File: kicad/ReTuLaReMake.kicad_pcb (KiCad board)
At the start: 2 copper layers, 54 x 26 mm, 23 parts, among them J1 40 Pin DIP Header, U1 ATF1508AS-10AU100

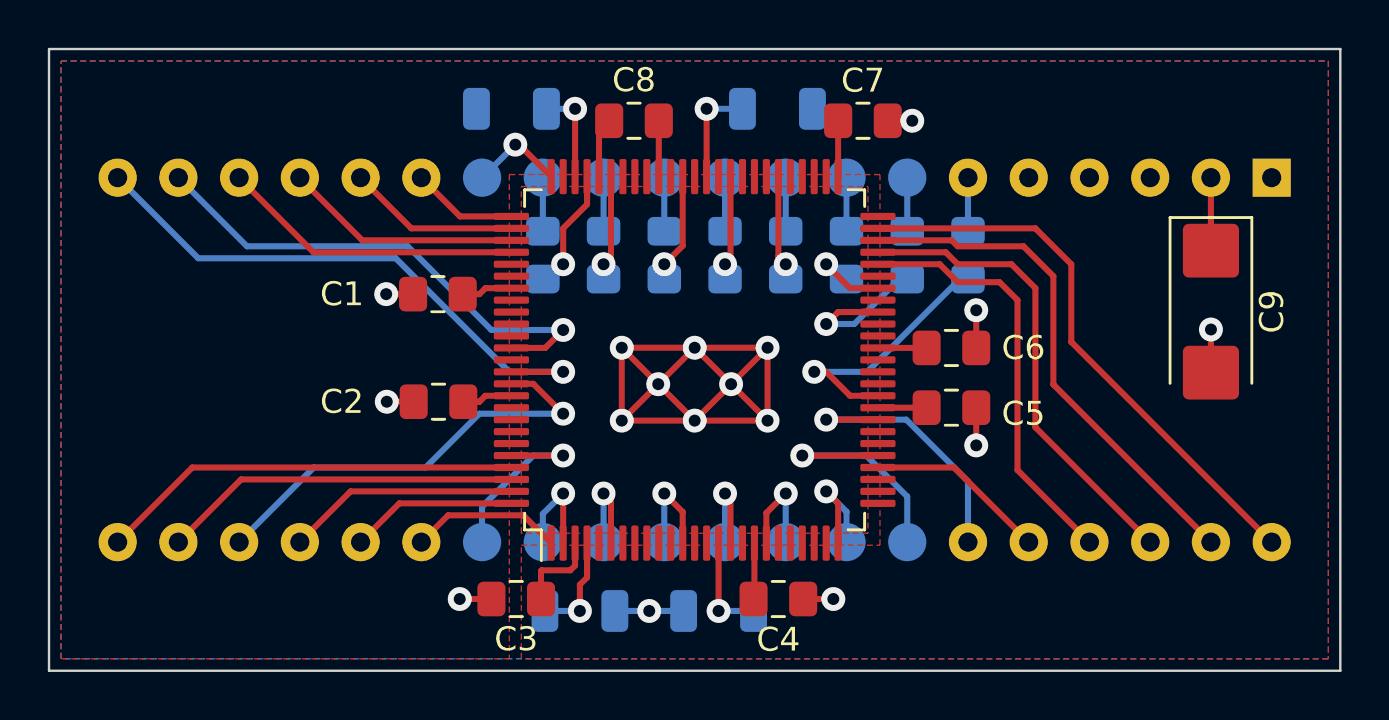
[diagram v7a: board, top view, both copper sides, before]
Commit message: KiCad: Move p_rd_b to a global clock
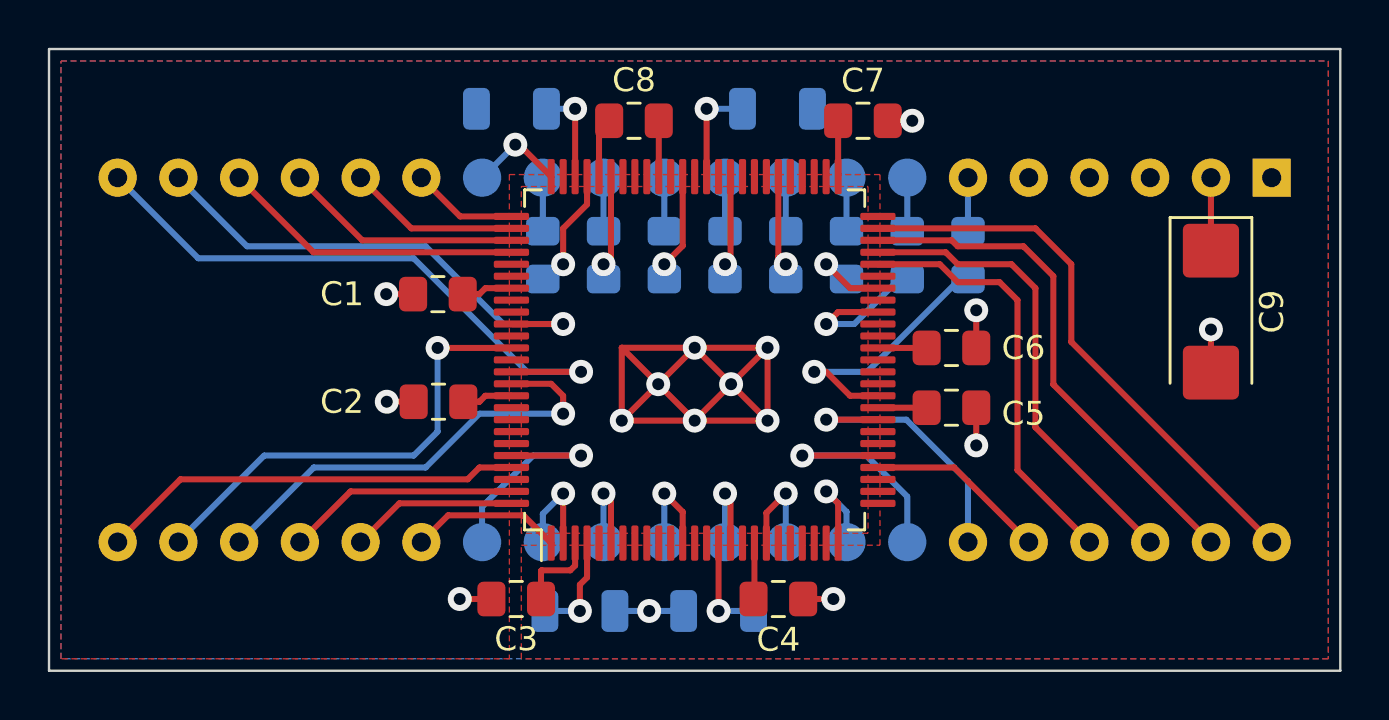
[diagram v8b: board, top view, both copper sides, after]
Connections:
- U1 pad 85: GND -> /HO2
- U1 pad 87: /HO2 -> /PNRDS
- U1 pad 98: /PNRDS -> GND
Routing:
- net /PNRDS: track 15.0 -> 19.4 mm, vias 0 -> 1
- net /PA0: track 7.92 -> 9.42 mm
- net /HRST: track 24.2 -> 25.7 mm
- net GND: vias 16 -> 15
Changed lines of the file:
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@@
   (net 46 "/HD6")
   (net 47 "/HD7")
-  (net 48 "Net-(U1-Pad62)")
-  (net 49 "Net-(U1-Pad73)")
+  (net 48 "Net-(R9-Pad1)")
+  (net 49 "Net-(R10-Pad1)")
   (net 50 "Net-(R11-Pad1)")
   (net 51 "unconnected-(R10-Pad2)")
@@
       (net 2 "GND") (pinfunction "I/O_47") (pintype "passive"))
     (pad "62" smd roundrect (at 7.6625 0.5 90) (size 1.475 0.3) (layers "F.Cu" "F.Paste" "F.Mask") (roundrect_rratio 0.25)
-      (net 48 "Net-(U1-Pad62)") (pinfunction "I/O/TCK") (pintype "passive"))
+      (net 48 "Net-(R9-Pad1)") (pinfunction "I/O/TCK") (pintype "passive"))
     (pad "63" smd roundrect (at 7.6625 0 90) (size 1.475 0.3) (layers "F.Cu" "F.Paste" "F.Mask") (roundrect_rratio 0.25)
       (net 2 "GND") (pinfunction "I/O_48") (pintype "passive"))
@@
       (net 47 "/HD7") (pinfunction "I/O_56") (pintype "passive"))
     (pad "73" smd roundrect (at 7.6625 -5 90) (size 1.475 0.3) (layers "F.Cu" "F.Paste" "F.Mask") (roundrect_rratio 0.25)
-      (net 49 "Net-(U1-Pad73)") (pinfunction "I/O/TDO") (pintype "passive"))
+      (net 49 "Net-(R10-Pad1)") (pinfunction "I/O/TDO") (pintype "passive"))
     (pad "74" smd roundrect (at 7.6625 -5.5 90) (size 1.475 0.3) (layers "F.Cu" "F.Paste" "F.Mask") (roundrect_rratio 0.25)
       (net 2 "GND") (pinfunction "GND_6") (pintype "passive"))
@@
       (net 2 "GND") (pinfunction "I/O_65") (pintype "passive"))
     (pad "85" smd roundrect (at 1.5 -7.6625 90) (size 0.3 1.475) (layers "F.Cu" "F.Paste" "F.Mask") (roundrect_rratio 0.25)
-      (net 2 "GND") (pinfunction "I/O/GCLK3") (pintype "passive"))
+      (net 18 "/HO2") (pinfunction "I/O/GCLK3") (pintype "passive"))
     (pad "86" smd roundrect (at 1 -7.6625 90) (size 0.3 1.475) (layers "F.Cu" "F.Paste" "F.Mask") (roundrect_rratio 0.25)
       (net 2 "GND") (pinfunction "GND_7") (pintype "passive"))
     (pad "87" smd roundrect (at 0.5 -7.6625 90) (size 0.3 1.475) (layers "F.Cu" "F.Paste" "F.Mask") (roundrect_rratio 0.25)
-      (net 18 "/HO2") (pinfunction "INPUT/GCLK1") (pintype "passive"))
+      (net 21 "/PNRDS") (pinfunction "INPUT/GCLK1") (pintype "passive"))
     (pad "88" smd roundrect (at 0 -7.6625 90) (size 0.3 1.475) (layers "F.Cu" "F.Paste" "F.Mask") (roundrect_rratio 0.25)
       (net 2 "GND") (pinfunction "INPUT/OE1") (pintype "passive"))
@@
       (net 20 "/PCS") (pinfunction "I/O_70") (pintype "passive"))
     (pad "98" smd roundrect (at -5 -7.6625 90) (size 0.3 1.475) (layers "F.Cu" "F.Paste" "F.Mask") (roundrect_rratio 0.25)
-      (net 21 "/PNRDS") (pinfunction "I/O_71") (pintype "passive"))
+      (net 2 "GND") (pinfunction "I/O_71") (pintype "passive"))
     (pad "99" smd roundrect (at -5.5 -7.6625 90) (size 0.3 1.475) (layers "F.Cu" "F.Paste" "F.Mask") (roundrect_rratio 0.25)
       (net 23 "/DACK") (pinfunction "I/O_72") (pintype "passive"))
@@
     (fp_line (start 1.6 0.8) (end 1.6 -0.8) (layer "B.Fab") (width 0.1))
     (pad "1" smd roundrect (at -1.4625 0 180) (size 1.125 1.75) (layers "B.Cu" "B.Paste" "B.Mask") (roundrect_rratio 0.2222222222)
-      (net 49 "Net-(U1-Pad73)") (pintype "passive"))
+      (net 49 "Net-(R10-Pad1)") (pintype "passive"))
     (pad "2" smd roundrect (at 1.4625 0 180) (size 1.125 1.75) (layers "B.Cu" "B.Paste" "B.Mask") (roundrect_rratio 0.2222222222)
       (net 51 "unconnected-(R10-Pad2)") (pintype "passive+no_connect"))
@@
     (fp_line (start 1.6 -0.8) (end -1.6 -0.8) (layer "B.Fab") (width 0.1))
     (pad "1" smd roundrect (at -1.4625 0) (size 1.125 1.75) (layers "B.Cu" "B.Paste" "B.Mask") (roundrect_rratio 0.2222222222)
-      (net 48 "Net-(U1-Pad62)") (pintype "passive"))
+      (net 48 "Net-(R9-Pad1)") (pintype "passive"))
     (pad "2" smd roundrect (at 1.4625 0) (size 1.125 1.75) (layers "B.Cu" "B.Paste" "B.Mask") (roundrect_rratio 0.2222222222)
       (net 2 "GND") (pintype "passive"))
@@
   (via (at 130.048 121.92) (size 1) (drill 0.5) (layers "F.Cu" "B.Cu") (free) (net 2))
   (via (at 136.1 109.38) (size 1) (drill 0.5) (layers "F.Cu" "B.Cu") (net 2))
-  (via (at 123.952 118.872) (size 1) (drill 0.5) (layers "F.Cu" "B.Cu") (free) (net 2))
   (via (at 128.524 120.396) (size 1) (drill 0.5) (layers "F.Cu" "B.Cu") (free) (net 2))
   (via (at 123.952 121.92) (size 1) (drill 0.5) (layers "F.Cu" "B.Cu") (free) (net 2))
@@
   (segment (start 107.945 111.765) (end 111.06 114.88) (width 0.254) (layer "F.Cu") (net 17))
   (segment (start 111.06 114.88) (end 119.3375 114.88) (width 0.254) (layer "F.Cu") (net 17))
-  (segment (start 121.5 118.13) (end 120.75 118.88) (width 0.254) (layer "F.Cu") (net 18))
-  (segment (start 120.75 118.88) (end 119.3375 118.88) (width 0.254) (layer "F.Cu") (net 18))
-  (via (at 121.5 118.13) (size 1) (drill 0.5) (layers "F.Cu" "B.Cu") (net 18))
-  (segment (start 115 114.63) (end 108.28 114.63) (width 0.254) (layer "B.Cu") (net 18))
-  (segment (start 121.5 118.13) (end 118.5 118.13) (width 0.254) (layer "B.Cu") (net 18))
-  (segment (start 118.5 118.13) (end 115 114.63) (width 0.254) (layer "B.Cu") (net 18))
+  (segment (start 121.5 117.88) (end 119.3375 117.88) (width 0.254) (layer "F.Cu") (net 18))
+  (via (at 121.5 117.88) (size 1) (drill 0.5) (layers "F.Cu" "B.Cu") (net 18))
+  (segment (start 121.5 117.88) (end 119 117.88) (width 0.254) (layer "B.Cu") (net 18))
+  (segment (start 119 117.88) (end 115.75 114.63) (width 0.254) (layer "B.Cu") (net 18))
   (segment (start 108.28 114.63) (end 105.41 111.76) (width 0.254) (layer "B.Cu") (net 18))
-  (segment (start 121.5 119.88) (end 119.3375 119.88) (width 0.254) (layer "F.Cu") (net 19))
-  (via (at 121.5 119.88) (size 1) (drill 0.5) (layers "F.Cu" "B.Cu") (net 19))
-  (segment (start 114.5 115.13) (end 119.25 119.88) (width 0.254) (layer "B.Cu") (net 19))
-  (segment (start 119.25 119.88) (end 121.5 119.88) (width 0.254) (layer "B.Cu") (net 19))
-  (segment (start 106.24 115.13) (end 114.5 115.13) (width 0.254) (layer "B.Cu") (net 19))
-  (segment (start 102.87 111.76) (end 106.24 115.13) (width 0.254) (layer "B.Cu") (net 19))
-  (segment (start 119.3375 123.88) (end 105.99 123.88) (width 0.254) (layer "F.Cu") (net 20))
-  (segment (start 102.865 127.005) (end 105.99 123.88) (width 0.254) (layer "F.Cu") (net 20))
-  (segment (start 108.03 124.38) (end 105.405 127.005) (width 0.254) (layer "F.Cu") (net 21))
-  (segment (start 119.3375 124.38) (end 108.03 124.38) (width 0.254) (layer "F.Cu") (net 21))
-  (segment (start 120.25 120.38) (end 119.3375 120.38) (width 0.254) (layer "F.Cu") (net 22))
-  (segment (start 121.5 121.63) (end 120.25 120.38) (width 0.254) (layer "F.Cu") (net 22))
+  (segment (start 115.75 114.63) (end 108.28 114.63) (width 0.254) (layer "B.Cu") (net 18))
+  (segment (start 122.25 119.88) (end 119.3375 119.88) (width 0.254) (layer "F.Cu") (net 19))
+  (via (at 122.25 119.88) (size 1) (drill 0.5) (layers "F.Cu" "B.Cu") (net 19))
+  (segment (start 106.24 115.13) (end 102.87 111.76) (width 0.254) (layer "B.Cu") (net 19))
+  (segment (start 120 119.88) (end 115.25 115.13) (width 0.254) (layer "B.Cu") (net 19))
+  (segment (start 122.25 119.88) (end 120 119.88) (width 0.254) (layer "B.Cu") (net 19))
+  (segment (start 115.25 115.13) (end 106.24 115.13) (width 0.254) (layer "B.Cu") (net 19))
+  (segment (start 105.495 124.375) (end 102.865 127.005) (width 0.254) (layer "F.Cu") (net 20))
+  (segment (start 119.3375 123.88) (end 118 123.88) (width 0.254) (layer "F.Cu") (net 20))
+  (segment (start 117.505 124.375) (end 105.495 124.375) (width 0.254) (layer "F.Cu") (net 20))
+  (segment (start 118 123.88) (end 117.505 124.375) (width 0.254) (layer "F.Cu") (net 20))
+  (segment (start 119.3375 118.88) (end 116.25 118.88) (width 0.254) (layer "F.Cu") (net 21))
+  (via (at 116.25 118.88) (size 1) (drill 0.5) (layers "F.Cu" "B.Cu") (net 21))
+  (segment (start 105.41 127) (end 105.41 126.97) (width 0.254) (layer "B.Cu") (net 21))
+  (segment (start 105.41 126.97) (end 109 123.38) (width 0.254) (layer "B.Cu") (net 21))
+  (segment (start 115.25 123.38) (end 116.25 122.38) (width 0.254) (layer "B.Cu") (net 21))
+  (segment (start 109 123.38) (end 115.25 123.38) (width 0.254) (layer "B.Cu") (net 21))
+  (segment (start 116.25 118.88) (end 116.25 122.38) (width 0.254) (layer "B.Cu") (net 21))
+  (segment (start 121 120.38) (end 119.3375 120.38) (width 0.254) (layer "F.Cu") (net 22))
+  (segment (start 121.5 120.88) (end 121 120.38) (width 0.254) (layer "F.Cu") (net 22))
+  (segment (start 121.5 121.63) (end 121.5 120.88) (width 0.254) (layer "F.Cu") (net 22))
   (via (at 121.5 121.63) (size 1) (drill 0.5) (layers "F.Cu" "B.Cu") (net 22))
   (segment (start 111.07 123.88) (end 107.95 127) (width 0.254) (layer "B.Cu") (net 22))
@@
   (segment (start 119.8375 125.88) (end 121 127.0425) (width 0.254) (layer "F.Cu") (net 25))
   (segment (start 116.69 125.88) (end 119.8375 125.88) (width 0.254) (layer "F.Cu") (net 25))
-  (segment (start 119.3375 123.38) (end 121.5 123.38) (width 0.254) (layer "F.Cu") (net 26))
-  (via (at 121.5 123.38) (size 1) (drill 0.5) (layers "F.Cu" "B.Cu") (net 26))
-  (segment (start 121.5 123.38) (end 120.25 123.38) (width 0.254) (layer "B.Cu") (net 26))
+  (segment (start 119.3375 123.38) (end 122.25 123.38) (width 0.254) (layer "F.Cu") (net 26))
+  (via (at 122.25 123.38) (size 1) (drill 0.5) (layers "F.Cu" "B.Cu") (net 26))
   (segment (start 118.11 125.52) (end 118.11 127) (width 0.254) (layer "B.Cu") (net 26))
+  (segment (start 122.25 123.38) (end 120.25 123.38) (width 0.254) (layer "B.Cu") (net 26))
   (segment (start 120.25 123.38) (end 118.11 125.52) (width 0.254) (layer "B.Cu") (net 26))
   (segment (start 121.5 124.968) (end 121.5 127.0425) (width 0.254) (layer "F.Cu") (net 27))
